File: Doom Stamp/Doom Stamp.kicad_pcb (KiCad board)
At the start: 2 copper layers, 31 x 32.5 mm, 47 parts, among them J1 USB_C_Receptacle_USB2.0, J6 USB_C_Receptacle_PowerOnly_6P, SW1 Conn_01x02, U1 NCP1117-3.3_SOT223, U2 W25Q128JVS, U3 RP2040, U4 ST7735s_8, U5 MAX98357AETE+T, Y1 ABLS-12.000MHZ-B4-T

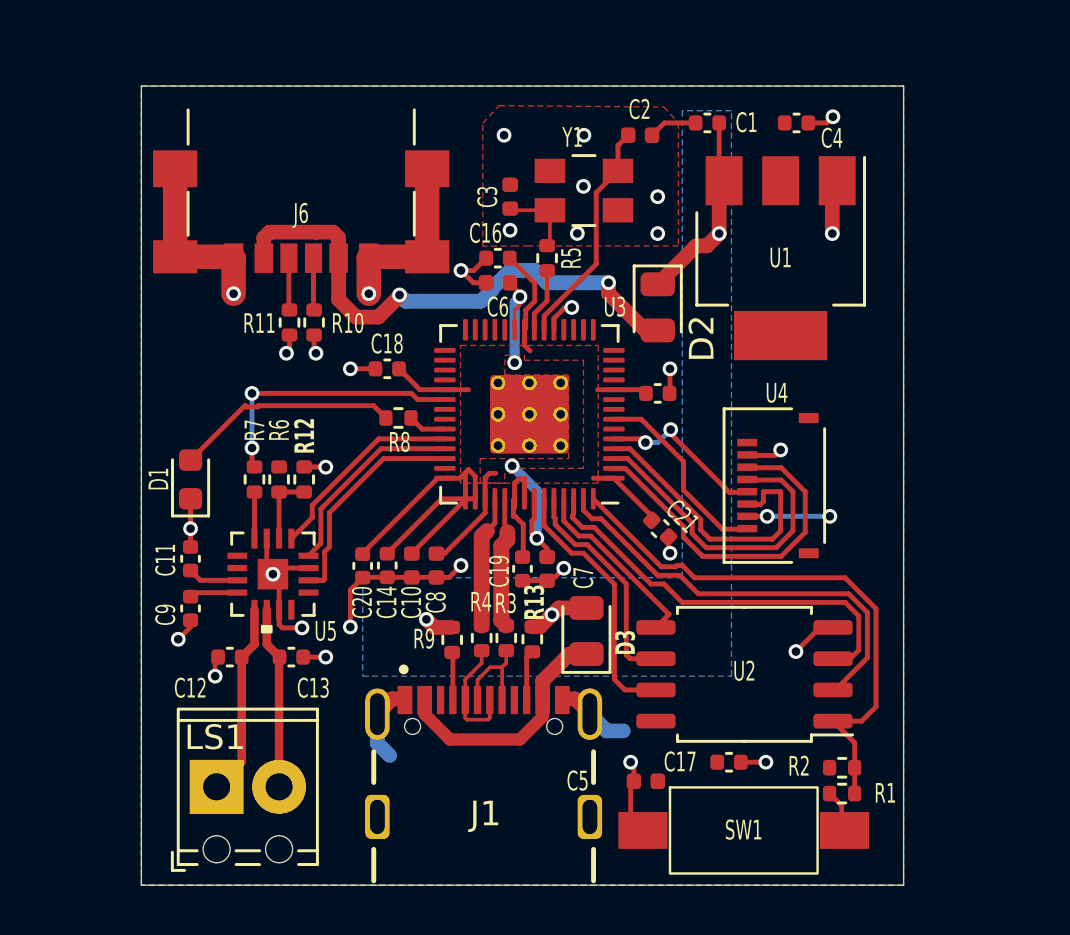
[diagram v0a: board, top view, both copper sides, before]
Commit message: add mounting holes
and some readme edits
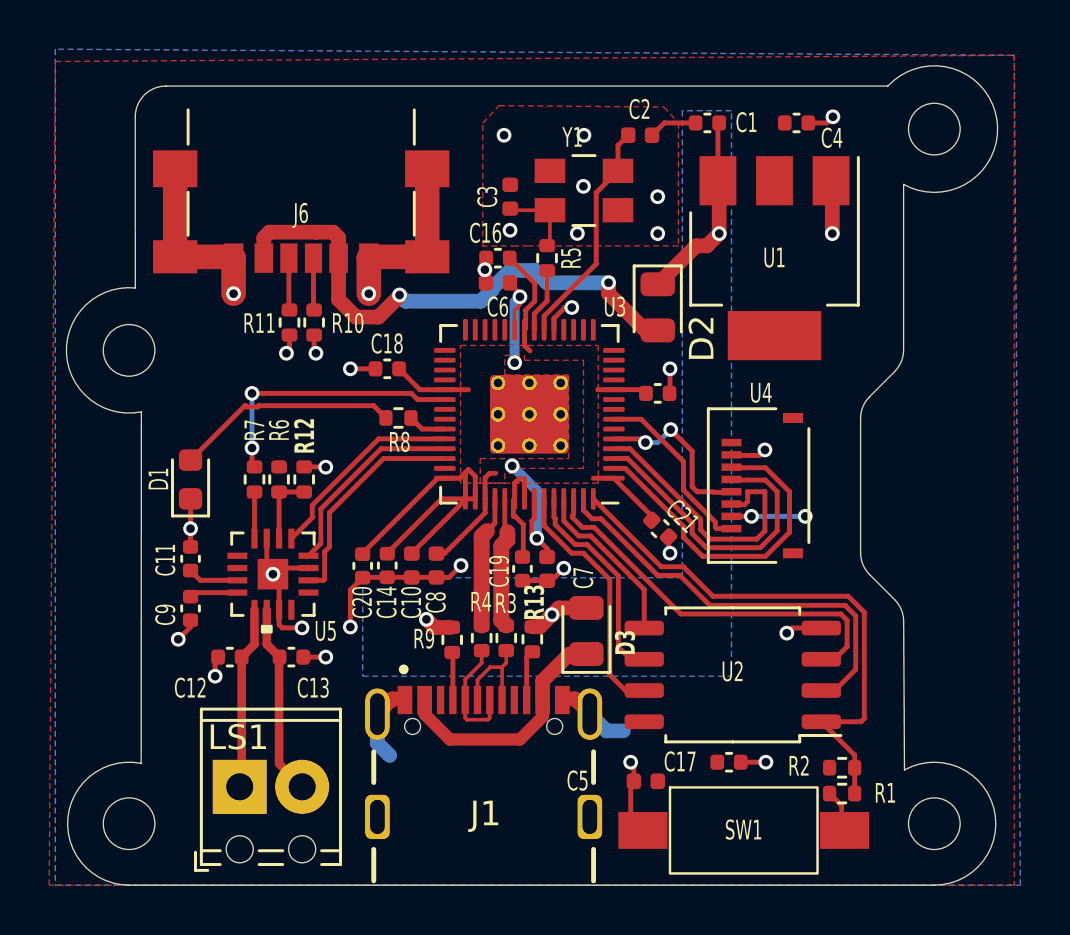
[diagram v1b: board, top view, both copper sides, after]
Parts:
- added REF**: MountingHole_2.1mm, MountingHole:MountingHole_2.1mm, F.Cu at (99.0, 148.5)
- added REF**: MountingHole_2.1mm, MountingHole:MountingHole_2.1mm, F.Cu at (131.8, 120.2)
- added REF**: MountingHole_2.1mm, MountingHole:MountingHole_2.1mm, F.Cu at (99.0, 129.2)
- added REF**: MountingHole_2.1mm, MountingHole:MountingHole_2.1mm, F.Cu at (131.8, 148.5)
- moved LS1 0.94 mm to (103.5, 147.0)
- moved U4 0.64 mm to (124.6, 134.8)
- moved U2 0.48 mm to (123.6, 142.4)
- moved U1 0.25 mm to (125.2, 125.5)
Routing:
- net GND: track 62.2 -> 60.3 mm
- net /QSPI_SD2: track 16.7 -> 16.0 mm
- net /GPIO2: track 12.1 -> 11.5 mm
- net /GPIO0: track 14.4 -> 13.7 mm
- net /GPIO1: track 13.0 -> 12.4 mm
- net /QSPI_SD0: track 7.51 -> 6.89 mm
- net VBUS: track 12.1 -> 11.5 mm
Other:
- board size 31 x 32.5 mm -> 37.9 x 33.3 mm

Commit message: update mounting holes
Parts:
- moved REF** 0.75 mm to (131.8, 121.0)
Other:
- board size 37.9 x 33.3 mm -> 37.8 x 32.5 mm
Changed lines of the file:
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@@
   )
   (footprint "MountingHole:MountingHole_2.1mm" (layer "F.Cu")
-    (at 131.75 120.25)
+    (at 131.75 121)
     (descr "Mounting Hole 2.1mm, no annular")
     (tags "mounting hole 2.1mm no annular")
@@
   (gr_line (start 128.75 138) (end 128.75 131.5)
     (stroke (width 0.1) (type default)) (layer "Dwgs.User"))
-  (gr_line (start 130.5 122.5) (end 130.5 129.232233)
-    (stroke (width 0.05) (type default)) (layer "Edge.Cuts"))
   (gr_line (start 131.75 151) (end 99 151)
     (stroke (width 0.05) (type default)) (layer "Edge.Cuts"))
@@
   (gr_line (start 99.253686 126.713144) (end 99.250561 119.750543)
     (stroke (width 0.05) (type default)) (layer "Edge.Cuts"))
-  (gr_line (start 100.500543 118.499982) (end 129.862955 118.499555)
-    (stroke (width 0.05) (type default)) (layer "Edge.Cuts"))
   (gr_line (start 129.116117 138.366117) (end 130.136712 139.386712)
     (stroke (width 0.05) (type default)) (layer "Edge.Cuts"))
   (gr_arc (start 99.250561 119.750543) (mid 99.616477 118.866301) (end 100.500543 118.499982)
     (stroke (width 0.05) (type default)) (layer "Edge.Cuts"))
-  (gr_arc (start 129.862955 118.499555) (mid 134.291879 119.845222) (end 130.5 122.5)
+  (gr_line (start 100.500543 118.499982) (end 131.75 118.5)
     (stroke (width 0.05) (type default)) (layer "Edge.Cuts"))
   (gr_line (start 99.49029 146.048548) (end 99.5 131.749999)
@@
   (gr_line (start 130.502809 140.263761) (end 130.535893 146.314607)
     (stroke (width 0.05) (type default)) (layer "Edge.Cuts"))
+  (gr_line (start 130.5 129.232233) (end 130.498694 123.164309)
+    (stroke (width 0.05) (type default)) (layer "Edge.Cuts"))
   (gr_arc (start 99 151) (mid 96.512167 148.253656) (end 99.49029 146.048548)
     (stroke (width 0.05) (type default)) (layer "Edge.Cuts"))
@@
   (gr_line (start 129.116117 131.133883) (end 130.133884 130.116116)
     (stroke (width 0.05) (type default)) (layer "Edge.Cuts"))
+  (gr_arc (start 131.75 118.5) (mid 134.164619 121.647776) (end 130.498694 123.164309)
+    (stroke (width 0.05) (type default)) (layer "Edge.Cuts"))
   (segment (start 105.1 139.8003) (end 105.1 140.4067) (width 0.2) (layer "F.Cu") (net 1))
